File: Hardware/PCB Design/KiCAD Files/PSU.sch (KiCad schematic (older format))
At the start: 10 parts, among them P10 5V, P11 3V3, P12 GND, U1 LM2575

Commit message: Update PCB
With notes from John
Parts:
- L1: footprint matts_components:C2V8_large_pads -> REInnovationFootprint:TH_Inductor
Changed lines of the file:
@@
 F 0 "L1" V 8150 1600 40  0000 C CNN
 F 1 "330uH" V 8300 1600 40  0000 C CNN
-F 2 "matts_components:C2V8_large_pads" H 8200 1600 60  0001 C CNN
+F 2 "REInnovationFootprint:TH_Inductor" H 8200 1600 60  0001 C CNN
 F 3 "http://docs-europe.electrocomponents.com/webdocs/0d90/0900766b80d90b31.pdf" H 8200 1600 60  0001 C CNN
 F 4 "Inductor. 1A RMS. " H 8200 1600 60  0001 C CNN "Description"

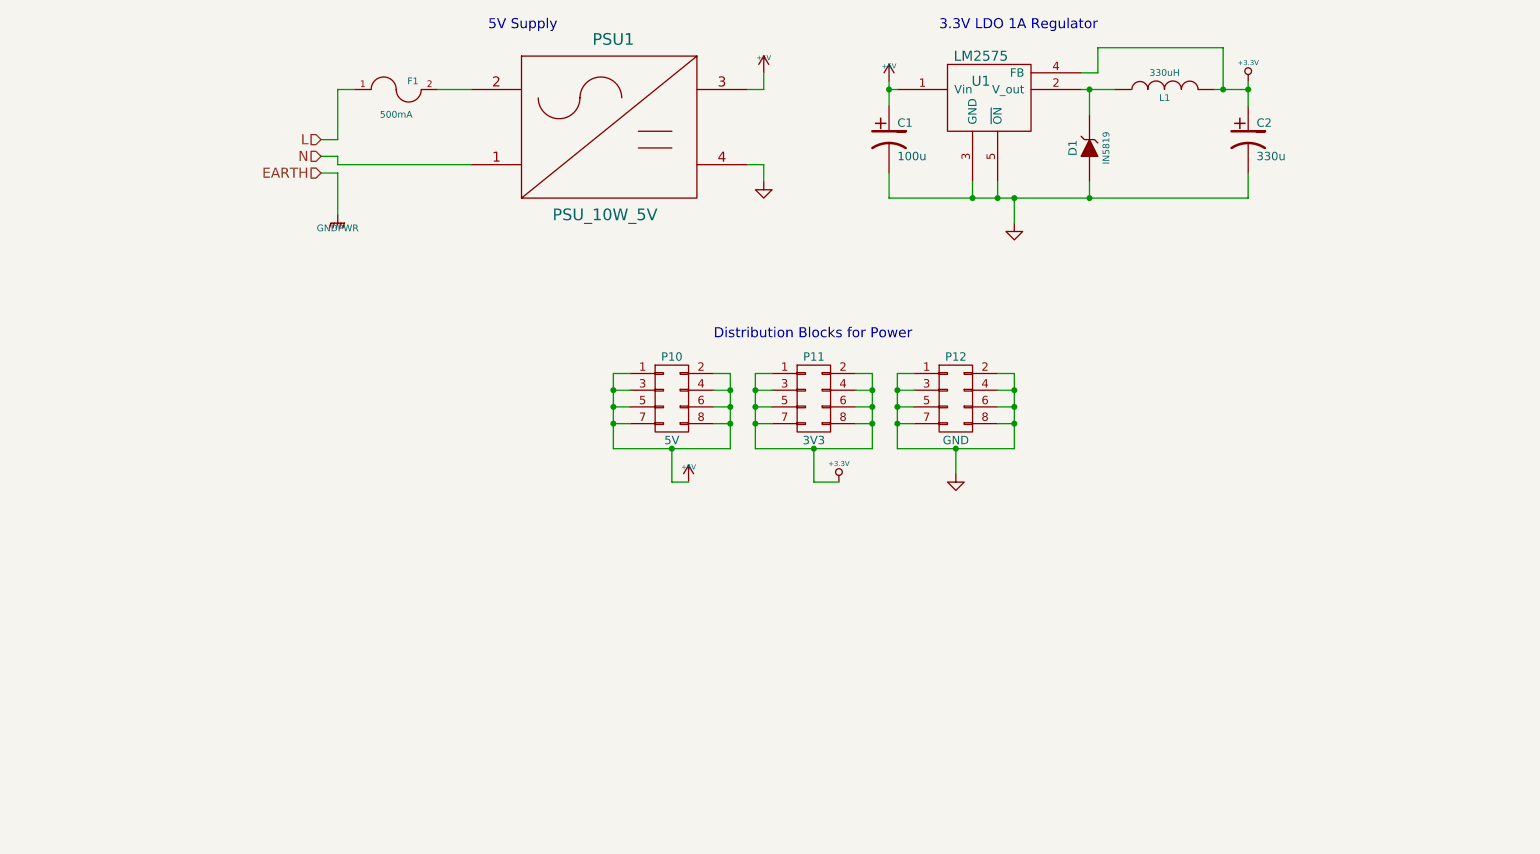
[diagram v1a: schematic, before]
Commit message: Version 3 revision
Added 3A switching 5V supply and Capacitors axial and radial
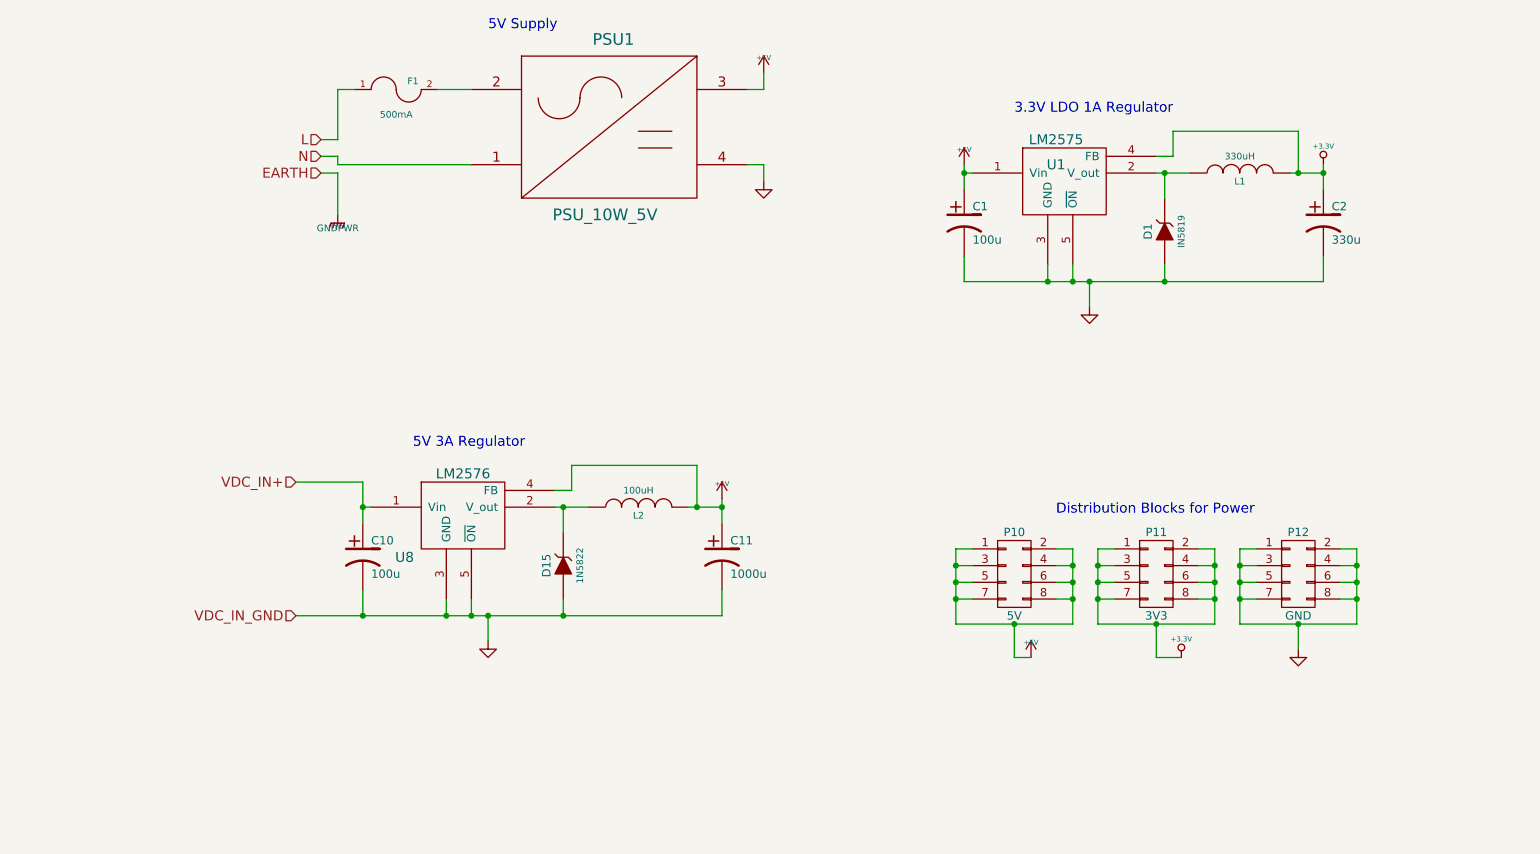
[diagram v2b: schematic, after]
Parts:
- added C10: 100u, REInnovationFootprint:C2V8_VandA, symbol CP1-RESCUE-oBeMs_Pulse_PCB
- added C11: 1000u, REInnovationFootprint:C2V8_VandA, symbol CP1-RESCUE-oBeMs_Pulse_PCB
- added D15: 1N5822, REInnovationFootprint:TH_Diode_DO-201AD, symbol ZENER-RESCUE-oBeMs_Pulse_PCB
- added L2: 100uH, REInnovationFootprint:TH_Inductor_ELC18B101L, symbol INDUCTOR
- added U8: LM2576, REInnovationFootprint:TO220_5PIN, symbol LM2576
- C1, C2: footprint matts_components:C2V8_large_pads -> REInnovationFootprint:C2V8_VandA
- P10, P11, P12: footprint Pin_Headers:Pin_Header_Straight_2x04 -> REInnovationFootprint:Pin_Header_Straight_2x04
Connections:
- net +5V: now also C11.1, L2.2, U8.4 (FB)
- net GND: now also C10.2, C11.2, D15.1 (A), U8.3 (GND), U8.5 (~ON)
- new net: D15.2 (K), L2.1, U8.2 (V_out)
- new net VDC_IN+: C10.1, U8.1 (Vin)
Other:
- note added: "5V 3A Regulator"
- moved on the sheet: C1, C2, D1, L1, P10, P11, P12, U1

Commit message: Updates from email 21/12/15
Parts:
- removed P10: 5V, REInnovationFootprint:Pin_Header_Straight_2x04, symbol CONN_02X04
- removed P11: 3V3, REInnovationFootprint:Pin_Header_Straight_2x04, symbol CONN_02X04
- removed P12: GND, REInnovationFootprint:Pin_Header_Straight_2x04, symbol CONN_02X04
- added D16: BRIDGE, REInnovationFootprint:TH_BridgeRect_8A, symbol BRIDGE
- added P10: 5V, REInnovationFootprint:Pin_Header_Straight_2x08, symbol CONN_02X08
- added P11: 3V3, REInnovationFootprint:Pin_Header_Straight_2x08, symbol CONN_02X08
- added P12: GND, REInnovationFootprint:Pin_Header_Straight_2x08, symbol CONN_02X08
- added P2: EXT_CAP, matts_components:SIL-2_wide_lg_pad, symbol CONN_01X02
- C2: value 330u -> 1000u
- D1: value IN5819 -> 1N5822; footprint REInnovationFootprint:TH_Diode_1 -> REInnovationFootprint:TH_Diode_DO-201AD; Description 1A 40V Shottky Diode -> 3A 40V Shottky Diode; Manufacturer Part No 1N5819RL -> 1N5822; Supplier 1 Part No 687-0754 -> 687-0877
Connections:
- net +3.3V: now also P11.1 (P1), P11.10 (P10), P11.11 (P11), P11.12 (P12), P11.13 (P13), P11.14 (P14), P11.15 (P15), P11.16 (P16), P11.2 (P2), P11.3 (P3), P11.4 (P4), P11.5 (P5), P11.6 (P6), P11.7 (P7), P11.8 (P8), P11.9 (P9)
- net +5V: now also P10.1 (P1), P10.10 (P10), P10.11 (P11), P10.12 (P12), P10.13 (P13), P10.14 (P14), P10.15 (P15), P10.16 (P16), P10.2 (P2), P10.3 (P3), P10.4 (P4), P10.5 (P5), P10.6 (P6), P10.7 (P7), P10.8 (P8), P10.9 (P9)
- net GND: now also D16.1 (-), P12.1 (P1), P12.10 (P10), P12.11 (P11), P12.12 (P12), P12.13 (P13), P12.14 (P14), P12.15 (P15), P12.16 (P16), P12.2 (P2), P12.3 (P3), P12.4 (P4), P12.5 (P5), P12.6 (P6), P12.7 (P7), P12.8 (P8), P12.9 (P9), P2.2 (P2)
- net VDC_IN+: no longer names the net of C10.1, U8.1 (Vin)
- net VDC_IN+: now also D16.3 (+), P2.1 (P1)
- new net VIN_A: D16.4
- new net VIN_B: D16.2
- no-connect marks 0 -> 1
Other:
- moved on the sheet: C10, C11, D15, L2, U8

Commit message: Rev 6. Final changes before PCB v0000 done
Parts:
- added P30: UNREG_DC, REInnovationFootprint:Pin_Header_Straight_2x03, symbol CONN_02X03
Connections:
- net at C10.1, D16.3 (+), P2.1 (P1)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: now also P30.1 (P1), P30.2 (P2), P30.3 (P3), P30.4 (P4), P30.5 (P5), P30.6 (P6)
- net +3.3V renamed +3V3
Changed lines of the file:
@@
 encoding utf-8
 Sheet 2 10
-Title "oBeMs Open Pulse Monitor Unit"
-Date "2015-12-22"
-Rev "5"
+Title "oBeMS Open Interface Board 0001"
+Date "2015-12-23"
+Rev "6"
 Comp "T4 Sustainability"
-Comment1 "PCB design by RE-Innovation"
+Comment1 "PCB design by T4 Sustainability/RE-Innovation"
 Comment2 ""
 Comment3 ""
@@
 $EndComp
 $Comp
-L +5V #PWR03
-U 1 1 5636114D
-P 5800 1500
-F 0 "#PWR03" H 5800 1590 20  0001 C CNN
-F 1 "+5V" H 5800 1590 30  0000 C CNN
-F 2 "" H 5800 1500 60  0000 C CNN
-F 3 "" H 5800 1500 60  0000 C CNN
-	1    5800 1500
-	1    0    0    -1
-$EndComp
-$Comp
-L GNDPWR #PWR04
+L GNDPWR #PWR014
 U 1 1 56361153
 P 3250 2350
-F 0 "#PWR04" H 3250 2400 40  0001 C CNN
+F 0 "#PWR014" H 3250 2400 40  0001 C CNN
 F 1 "GNDPWR" H 3250 2270 40  0000 C CNN
 F 2 "" H 3250 2350 60  0000 C CNN
@@
 Text Notes 4150 1250 0    60   ~ 0
 5V Supply
-$Comp
-L GND-RESCUE-oBeMs_Pulse_PCB #PWR05
-U 1 1 5636115A
-P 5800 2150
-F 0 "#PWR05" H 5800 2150 30  0001 C CNN
-F 1 "GND" H 5800 2080 30  0001 C CNN
-F 2 "" H 5800 2150 60  0000 C CNN
-F 3 "" H 5800 2150 60  0000 C CNN
-	1    5800 2150
-	1    0    0    -1
-$EndComp
 Wire Wire Line
 	4050 1600 3850 1600
@@
 	3250 2100 3250 2350
 Wire Wire Line
-	5800 2050 5800 2150
-Wire Wire Line
-	5700 2050 5800 2050
-Wire Wire Line
-	5700 1600 5800 1600
-Wire Wire Line
-	5800 1600 5800 1500
+	5700 2050 6000 2050
+Wire Wire Line
+	5700 1600 6000 1600
 Text HLabel 3150 1900 0    60   Input ~ 0
 L
@@
 F 11 "Value" H 7000 2400 60  0001 C CNN "Supplier 2 Part No"
 	1    7000 2400
-	1    0    0    -1
-$EndComp
-$Comp
-L GND-RESCUE-oBeMs_Pulse_PCB #PWR06
-U 1 1 56363C28
-P 7750 2900
-F 0 "#PWR06" H 7750 2900 30  0001 C CNN
-F 1 "GND" H 7750 2830 30  0001 C CNN
-F 2 "" H 7750 2900 60  0000 C CNN
-F 3 "" H 7750 2900 60  0000 C CNN
-	1    7750 2900
-	1    0    0    -1
-$EndComp
-$Comp
-L +3.3V-RESCUE-oBeMs_Pulse_PCB #PWR07
-U 1 1 56363C2E
-P 9150 2050
-F 0 "#PWR07" H 9150 2010 30  0001 C CNN
-F 1 "+3.3V" H 9150 2160 30  0000 C CNN
-F 2 "" H 9150 2050 60  0000 C CNN
-F 3 "" H 9150 2050 60  0000 C CNN
-	1    9150 2050
-	1    0    0    -1
-$EndComp
-$Comp
-L +5V #PWR08
-U 1 1 56363C34
-P 7000 2050
-F 0 "#PWR08" H 7000 2140 20  0001 C CNN
-F 1 "+5V" H 7000 2140 30  0000 C CNN
-F 2 "" H 7000 2050 60  0000 C CNN
-F 3 "" H 7000 2050 60  0000 C CNN
-	1    7000 2050
 	1    0    0    -1
 $EndComp
@@
 $EndComp
 Wire Wire Line
-	9150 2050 9150 2200
-Wire Wire Line
-	7000 2050 7000 2200
+	9150 2000 9150 2200
+Wire Wire Line
+	7000 2000 7000 2200
 Wire Wire Line
 	7000 2600 7000 2750
@@
 Connection ~ 9150 2100
 Connection ~ 9000 2100
-$Comp
-L GND-RESCUE-oBeMs_Pulse_PCB #PWR09
-U 1 1 56364B88
-P 9000 4950
-F 0 "#PWR09" H 9000 4950 30  0001 C CNN
-F 1 "GND" H 9000 4880 30  0001 C CNN
-F 2 "" H 9000 4950 60  0000 C CNN
-F 3 "" H 9000 4950 60  0000 C CNN
-	1    9000 4950
-	1    0    0    -1
-$EndComp
-$Comp
-L +3.3V-RESCUE-oBeMs_Pulse_PCB #PWR010
-U 1 1 56364B8E
-P 8300 5000
-F 0 "#PWR010" H 8300 4960 30  0001 C CNN
-F 1 "+3.3V" H 8300 5110 30  0000 C CNN
-F 2 "" H 8300 5000 60  0000 C CNN
-F 3 "" H 8300 5000 60  0000 C CNN
-	1    8300 5000
-	1    0    0    -1
-$EndComp
-$Comp
-L +5V #PWR011
-U 1 1 56364B94
-P 7400 5000
-F 0 "#PWR011" H 7400 5090 20  0001 C CNN
-F 1 "+5V" H 7400 5090 30  0000 C CNN
-F 2 "" H 7400 5000 60  0000 C CNN
-F 3 "" H 7400 5000 60  0000 C CNN
-	1    7400 5000
-	1    0    0    -1
-$EndComp
 Text Notes 7600 3300 0    60   ~ 0
 Distribution Blocks for Power
@@
 F 11 "Value" H 4300 5000 60  0001 C CNN "Supplier 2 Part No"
 	1    4300 5000
-	1    0    0    -1
-$EndComp
-$Comp
-L GND-RESCUE-oBeMs_Pulse_PCB #PWR012
-U 1 1 56729E51
-P 5050 5500
-F 0 "#PWR012" H 5050 5500 30  0001 C CNN
-F 1 "GND" H 5050 5430 30  0001 C CNN
-F 2 "" H 5050 5500 60  0000 C CNN
-F 3 "" H 5050 5500 60  0000 C CNN
-	1    5050 5500
-	1    0    0    -1
-$EndComp
-$Comp
-L +5V #PWR013
-U 1 1 56729E5D
-P 6450 4650
-F 0 "#PWR013" H 6450 4740 20  0001 C CNN
-F 1 "+5V" H 6450 4740 30  0000 C CNN
-F 2 "" H 6450 4650 60  0000 C CNN
-F 3 "" H 6450 4650 60  0000 C CNN
-	1    6450 4650
 	1    0    0    -1
 $EndComp
@@
 	2750 5850 2750 5750
 Wire Wire Line
-	3600 4900 3600 4550
+	3600 3400 3600 4900
 Wire Wire Line
 	1900 4900 1900 6100
@@
 	0    -1   -1   0
 $EndComp
+$Comp
+L CONN_02X03 P30
+U 1 1 567A8A85
+P 3650 3050
+F 0 "P30" H 3650 3250 50  0000 C CNN
+F 1 "UNREG_DC" H 3650 2850 50  0000 C CNN
+F 2 "REInnovationFootprint:Pin_Header_Straight_2x03" H 3650 1850 50  0001 C CNN
+F 3 "" H 3650 1850 50  0000 C CNN
+	1    3650 3050
+	1    0    0    -1
+$EndComp
+Wire Wire Line
+	3400 2950 3050 2950
+Wire Wire Line
+	3050 2950 3050 3400
+Wire Wire Line
+	3050 3400 4050 3400
+Wire Wire Line
+	4050 3400 4050 2950
+Wire Wire Line
+	4050 2950 3900 2950
+Wire Wire Line
+	3900 3050 4050 3050
+Connection ~ 4050 3050
+Wire Wire Line
+	3900 3150 4050 3150
+Connection ~ 4050 3150
+Wire Wire Line
+	3400 3050 3050 3050
+Connection ~ 3050 3050
+Wire Wire Line
+	3400 3150 3050 3150
+Connection ~ 3050 3150
+Connection ~ 3600 3400
+Connection ~ 3600 4550
+Text HLabel 6000 1600 2    60   Output ~ 0
++5V
+Text HLabel 6750 2000 0    60   Input ~ 0
++5V
+Text HLabel 9300 2000 2    60   Output ~ 0
++3V3
+Text HLabel 6550 4650 2    60   Output ~ 0
++5V
+Text HLabel 7400 5000 2    60   Input ~ 0
++5V
+Text HLabel 8300 5000 2    60   Input ~ 0
++3V3
+Text HLabel 6000 2050 2    60   Output ~ 0
+GND
+Wire Wire Line
+	6750 2000 7000 2000
+Wire Wire Line
+	9150 2000 9300 2000
+Text HLabel 7750 2900 0    60   Input ~ 0
+GND
+Text HLabel 9000 4950 0    60   Input ~ 0
+GND
+Wire Wire Line
+	6450 4650 6550 4650
+Text HLabel 5050 5500 0    60   Input ~ 0
+GND
 $EndSCHEMATC

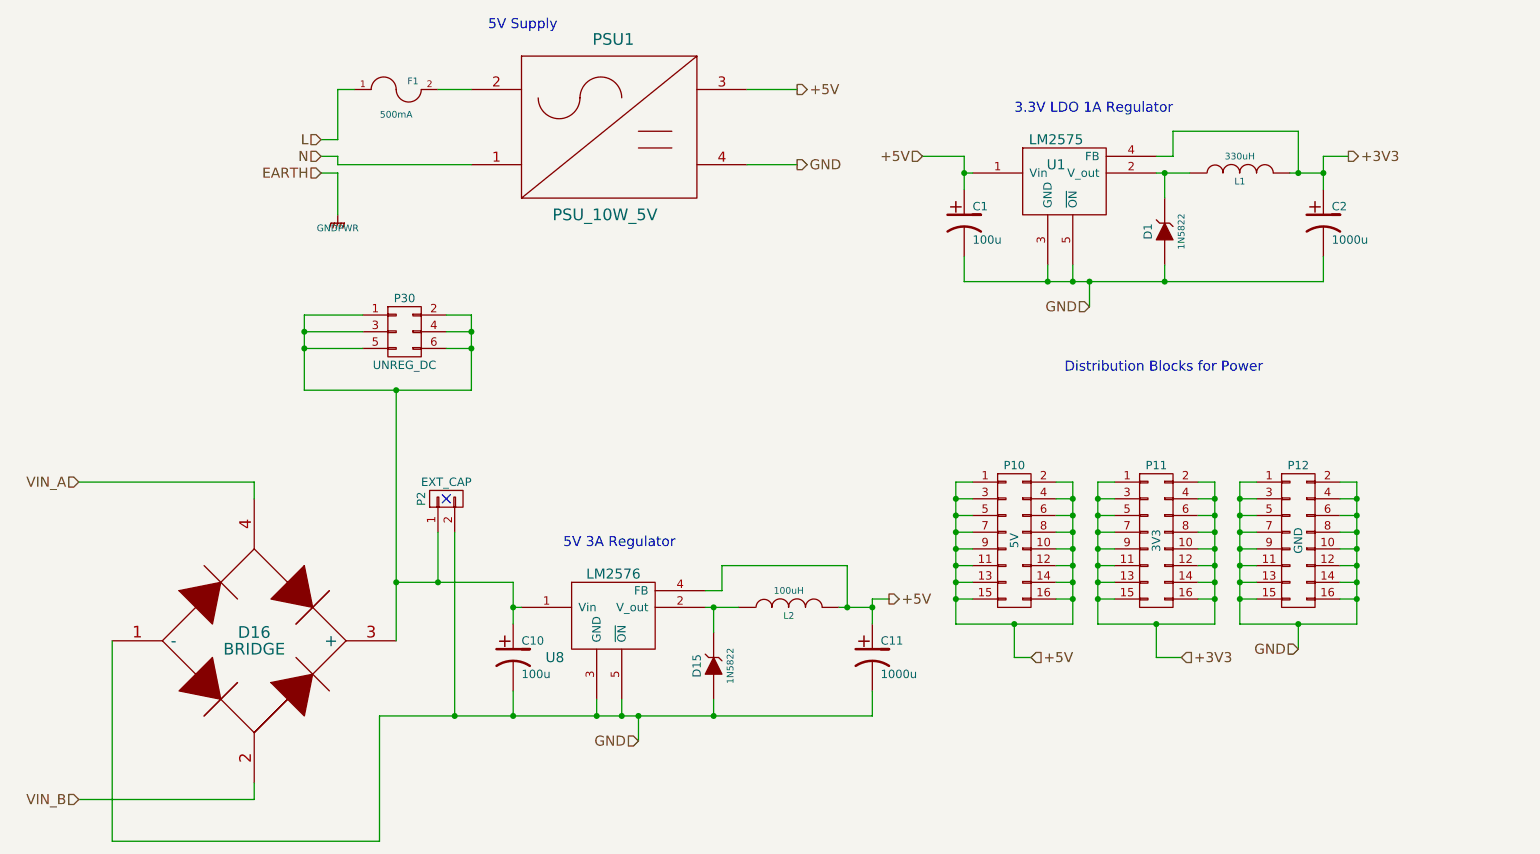
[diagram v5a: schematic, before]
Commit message: Changes for v0001
Multiple PCb changes. 50Pcs ordered
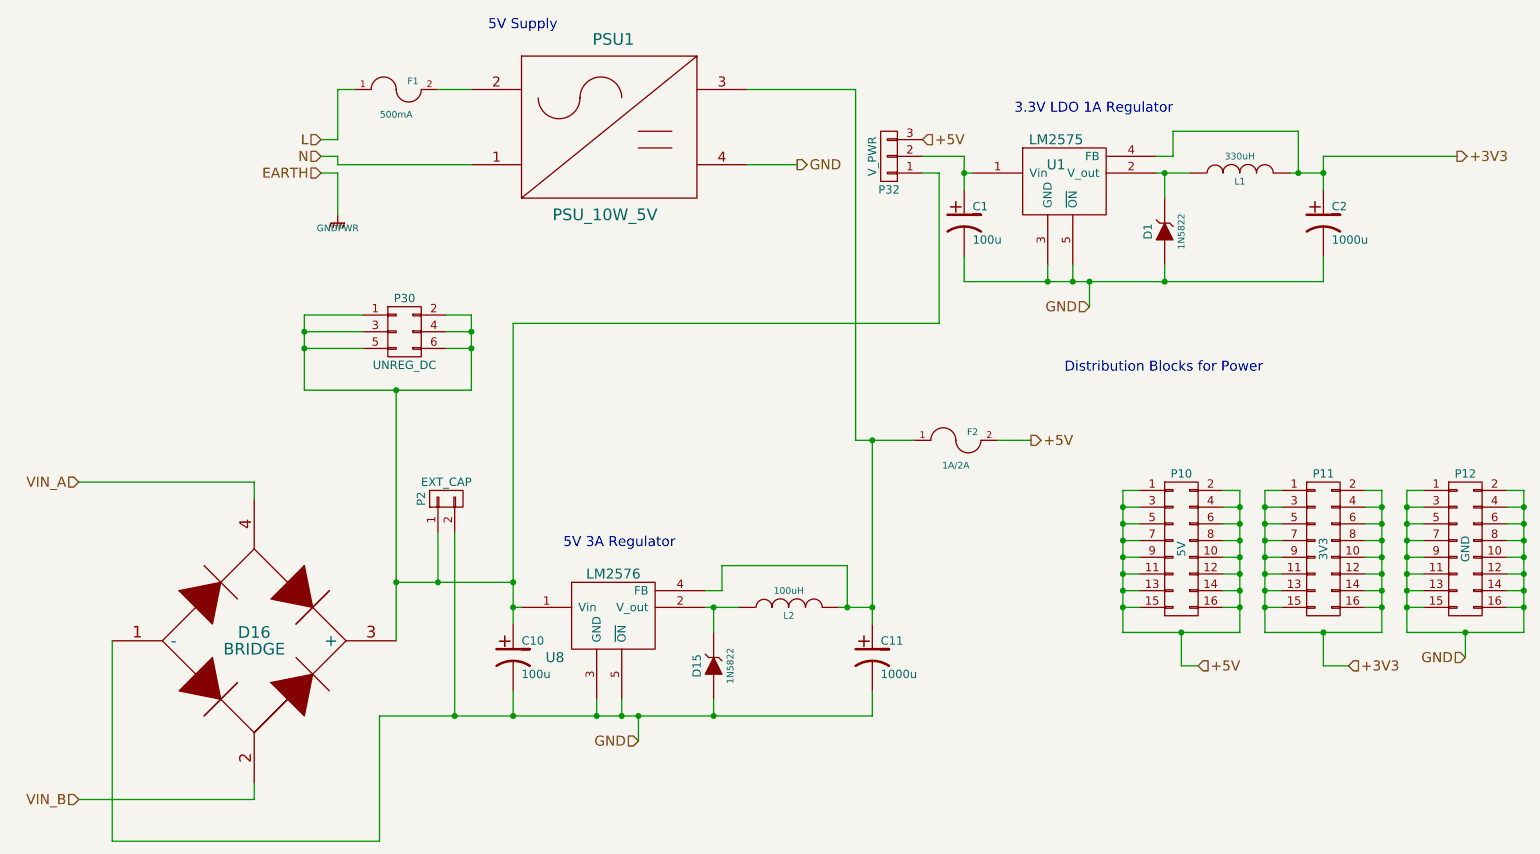
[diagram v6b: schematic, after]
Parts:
- added F2: 1A/2A, REInnovationFootprint:TH_Fuse_Holder_5-20_CPC, symbol FUSE
- added P32: V_PWR, REInnovationFootprint:SM_3pad_SOLDER_named, symbol CONN_01X03
- C1, C10, C11, C2: footprint REInnovationFootprint:C2V8_VandA -> REInnovationFootprint:C2V8_V
- P2: footprint matts_components:SIL-2_wide_lg_pad -> REInnovationFootprint:SIL-2_LG_PAD
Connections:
- net +5V: now also F2.2, P32.3 (P3); no longer C1.1, C11.1, L2.2, PSU1.3 (+5V), U1.1 (Vin), U8.4 (FB)
- net at C10.1, D16.3 (+), P2.1 (P1)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: now also P32.1 (P1)
- new net: C11.1, F2.1, L2.2, PSU1.3 (+5V), U8.4 (FB)
- new net: C1.1, P32.2 (P2), U1.1 (Vin)
- no-connect marks 1 -> 0
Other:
- moved on the sheet: P10, P11, P12
